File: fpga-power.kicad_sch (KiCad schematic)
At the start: 81 parts, among them U15 XC7K160T-FFG676

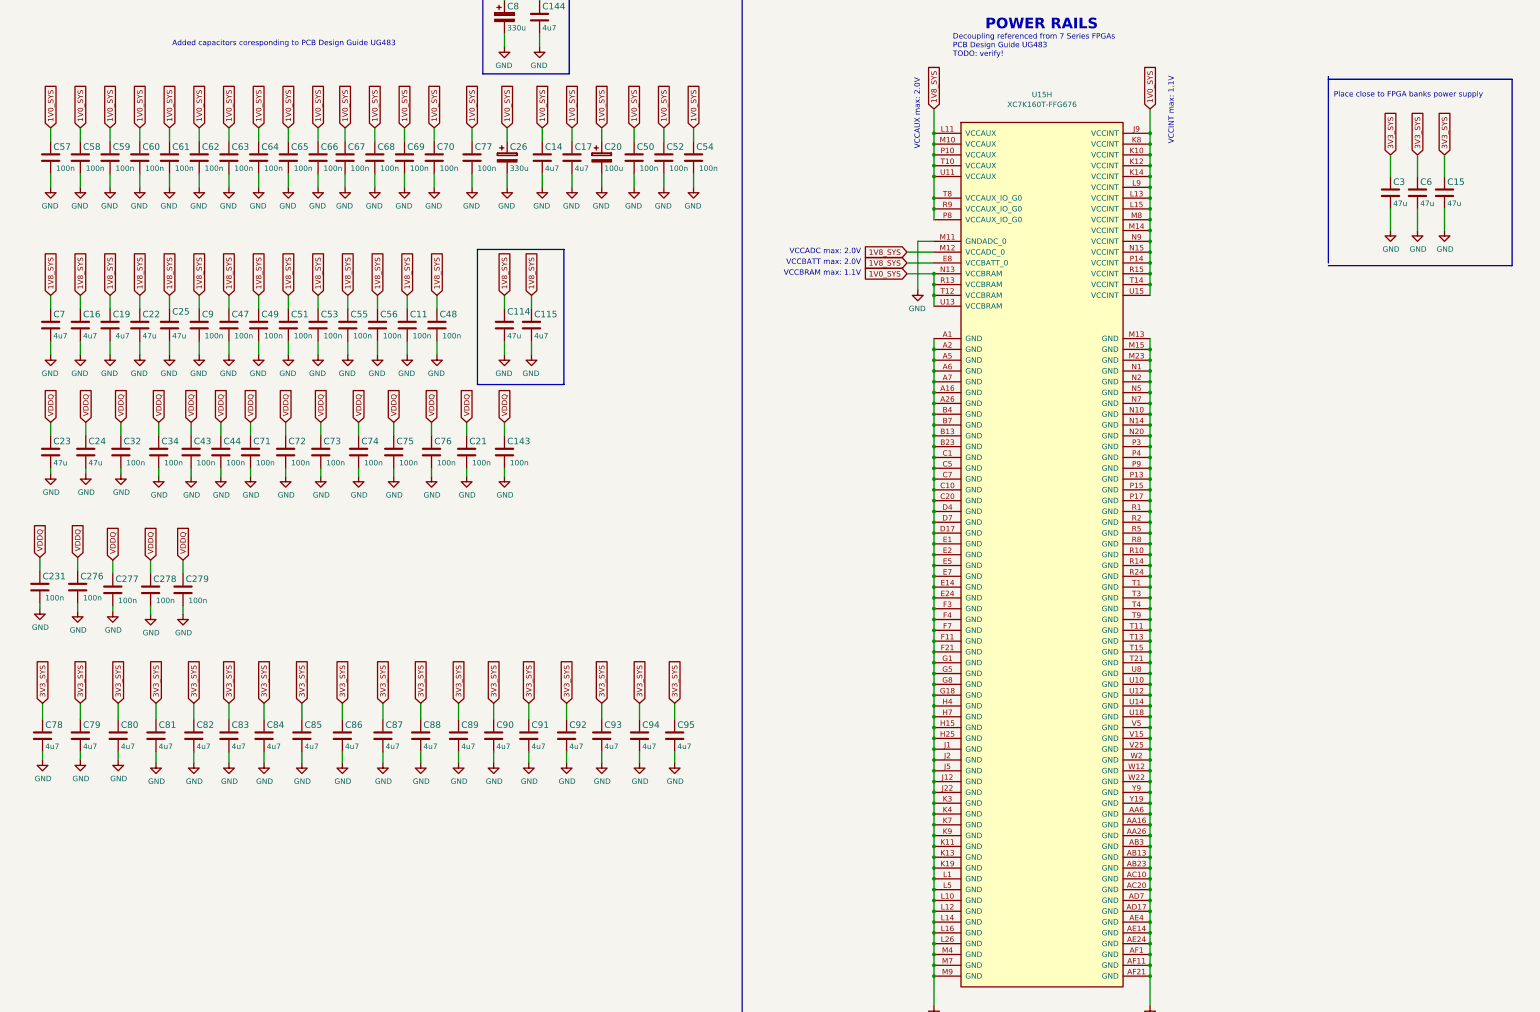
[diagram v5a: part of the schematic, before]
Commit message: Assign and connect misc. signals. Add, place and route decoupling capacitors
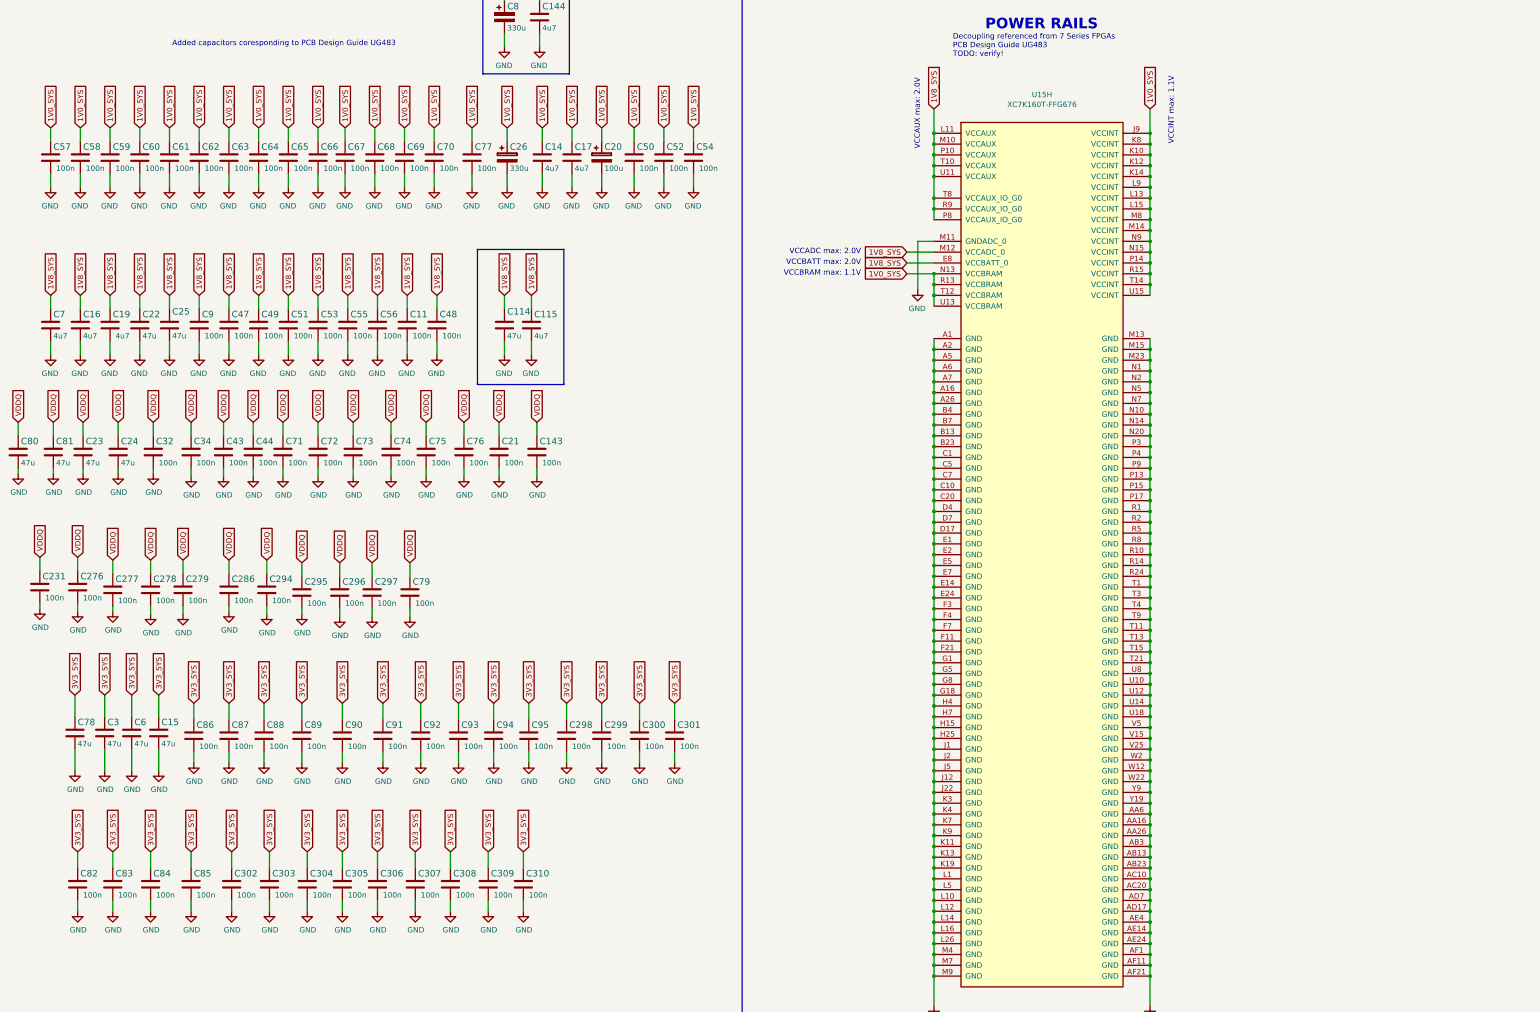
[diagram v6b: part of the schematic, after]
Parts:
- removed C78, C79, C80, C81, C82, C83, C84, C85, C86, C87, C88, C89, C90, C91, C92, C93, C94, C95: C_4u7_0402, data-center-dram-tester-footprints:0402-cap, symbol data-center-dram-tester:C_4u7_0402
- added C286, C294, C295, C296, C297, C298, C299, C300, C301, C302, C303, C304, C305, C306, C307, C308, C309, C310, C79, C82, C83, C84, C85, C86, C87, C88, C89, C90, C91, C92, C93, C94, C95: C_100n_0201, data-center-dram-tester-footprints:0201-res, symbol data-center-dram-tester:C_100n_0201
- added C78, C80, C81: C_47u_0603, data-center-dram-tester-footprints:0603-cap, symbol data-center-dram-tester:C_47u_0603
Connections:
- net 3V3_SYS: now also C298.1, C299.1, C300.1, C301.1, C302.1, C303.1, C304.1, C305.1, C306.1, C307.1, C308.1, C309.1, C310.1, C78.1, C82.1, C83.1, C84.1, C85.1, C86.1, C87.1, C88.1, C89.1, C90.1, C91.1, C92.1, C93.1, C94.1, C95.1
- net GND: now also C286.2, C294.2, C295.2, C296.2, C297.2, C298.2, C299.2, C300.2, C301.2, C302.2, C303.2, C304.2, C305.2, C306.2, C307.2, C308.2, C309.2, C310.2, C78.2, C79.2, C80.2, C81.2, C82.2, C83.2, C84.2, C85.2, C86.2, C87.2, C88.2, C89.2, C90.2, C91.2, C92.2, C93.2, C94.2, C95.2
- net VDDQ: now also C286.1, C294.1, C295.1, C296.1, C297.1, C79.1, C80.1, C81.1
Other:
- note removed: "Place close to FPGA banks power supply"
- moved on the sheet: C143, C15, C21, C23, C24, C3, C32, C34, C43, C44, C6, C71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

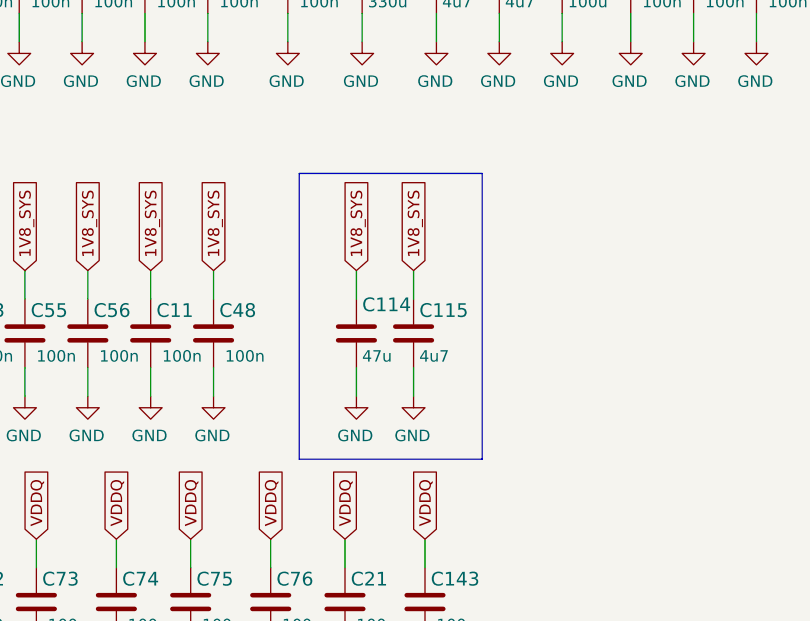
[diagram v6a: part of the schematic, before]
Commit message: Readability improvements
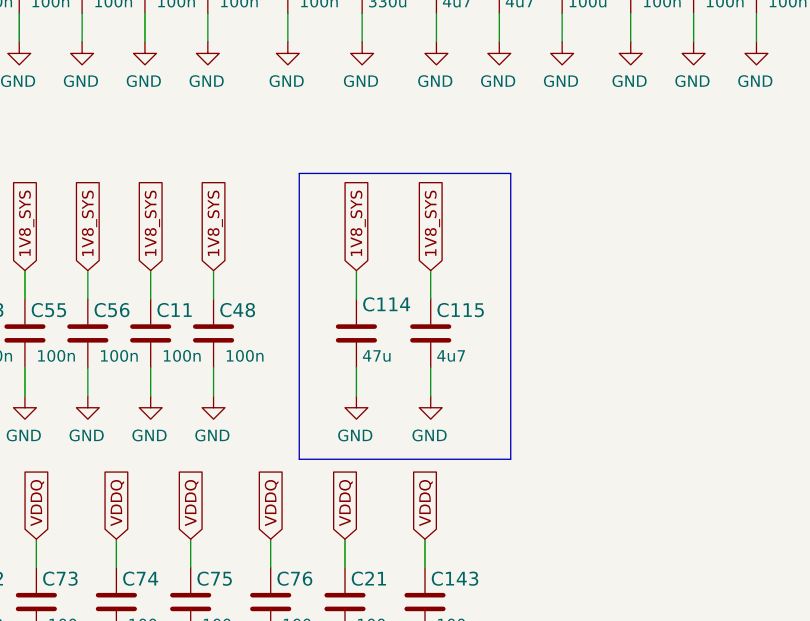
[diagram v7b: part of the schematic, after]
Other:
- moved on the sheet: C115
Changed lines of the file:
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@@
     (stroke (width 0) (type default) (color 0 0 0 0))
   )
-  (polyline (pts (xy 128.905 90.17) (xy 149.225 90.17))
+  (polyline (pts (xy 128.905 90.17) (xy 152.4 90.17))
     (stroke (width 0) (type default) (color 0 0 0 0))
   )
@@
     (stroke (width 0) (type default) (color 0 0 0 0))
   )
-  (polyline (pts (xy 149.225 121.92) (xy 128.905 121.92))
+  (polyline (pts (xy 152.4 121.92) (xy 128.905 121.92))
     (stroke (width 0) (type default) (color 0 0 0 0))
   )
@@
     (stroke (width 0) (type default) (color 0 0 0 0))
   )
-  (wire (pts (xy 141.605 104.14) (xy 141.605 100.965))
+  (wire (pts (xy 143.51 104.14) (xy 143.51 100.965))
     (stroke (width 0) (type default) (color 0 0 0 0))
   )
@@
     (stroke (width 0) (type default) (color 0 0 0 0))
   )
-  (polyline (pts (xy 149.225 90.17) (xy 149.225 121.92))
+  (polyline (pts (xy 152.4 90.17) (xy 152.4 121.92))
     (stroke (width 0) (type default) (color 0 0 0 0))
   )
@@
     (stroke (width 0) (type default) (color 0 0 0 0))
   )
-  (wire (pts (xy 141.605 114.935) (xy 141.605 111.76))
+  (wire (pts (xy 143.51 114.935) (xy 143.51 111.76))
     (stroke (width 0) (type default) (color 0 0 0 0))
   )
@@
     )
   )
-  (global_label "1V8_SYS" (shape input) (at 141.605 100.965 90) (fields_autoplaced)
+  (global_label "1V8_SYS" (shape input) (at 143.51 100.965 90) (fields_autoplaced)
     (effects (font (size 1.27 1.27)) (justify left))
-    (property "Intersheet References" "${INTERSHEET_REFS}" (id 0) (at -0.635 -45.72 0)
+    (property "Intersheet References" "${INTERSHEET_REFS}" (id 0) (at 1.27 -45.72 0)
       (effects (font (size 1.27 1.27)) hide)
     )
@@
     (pin "1")
   )
-  (symbol (lib_id "data-center-dram-tester:C_4u7_0402") (at 141.605 107.95 0) (unit 1)
+  (symbol (lib_id "data-center-dram-tester:C_4u7_0402") (at 143.51 107.95 0) (unit 1)
     (in_bom yes) (on_board yes)
-    (property "Reference" "C115" (id 0) (at 142.24 105.41 0)
+    (property "Reference" "C115" (id 0) (at 144.145 105.41 0)
       (effects (font (size 1.524 1.524)) (justify left))
     )
-    (property "Value" "C_4u7_0402" (id 1) (at 141.605 111.76 0)
+    (property "Value" "C_4u7_0402" (id 1) (at 143.51 111.76 0)
       (effects (font (size 1.524 1.524)) hide)
     )
-    (property "Footprint" "data-center-dram-tester-footprints:0402-cap" (id 2) (at 146.685 102.87 0)
+    (property "Footprint" "data-center-dram-tester-footprints:0402-cap" (id 2) (at 148.59 102.87 0)
       (effects (font (size 1.524 1.524)) (justify left) hide)
     )
-    (property "Datasheet" "" (id 3) (at 141.605 107.95 0)
+    (property "Datasheet" "" (id 3) (at 143.51 107.95 0)
       (effects (font (size 1.27 1.27)) hide)
     )
-    (property "Manufacturer" "MURATA" (id 4) (at 146.685 97.79 0)
+    (property "Manufacturer" "MURATA" (id 4) (at 148.59 97.79 0)
       (effects (font (size 1.524 1.524)) (justify left) hide)
     )
-    (property "MPN" "GRM155R61A475MEAAD" (id 5) (at 146.685 100.33 0)
+    (property "MPN" "GRM155R61A475MEAAD" (id 5) (at 148.59 100.33 0)
       (effects (font (size 1.524 1.524)) (justify left) hide)
     )
-    (property "Val" "4u7" (id 6) (at 142.24 110.49 0)
+    (property "Val" "4u7" (id 6) (at 144.145 110.49 0)
       (effects (font (size 1.27 1.27)) (justify left))
     )
@@
     (pin "2")
   )
-  (symbol (lib_id "data-center-dram-tester:GND") (at 141.605 114.935 0) (mirror y) (unit 1)
+  (symbol (lib_id "data-center-dram-tester:GND") (at 143.51 114.935 0) (mirror y) (unit 1)
     (in_bom yes) (on_board yes)
-    (property "Reference" "#PWR0108" (id 0) (at 141.605 121.285 0)
+    (property "Reference" "#PWR0108" (id 0) (at 143.51 121.285 0)
       (effects (font (size 1.27 1.27)) hide)
     )
-    (property "Value" "GND" (id 1) (at 141.478 119.3292 0))
-    (property "Footprint" "" (id 2) (at 141.605 114.935 0)
+    (property "Value" "GND" (id 1) (at 143.383 119.3292 0))
+    (property "Footprint" "" (id 2) (at 143.51 114.935 0)
       (effects (font (size 1.27 1.27)) hide)
     )
-    (property "Datasheet" "" (id 3) (at 141.605 114.935 0)
+    (property "Datasheet" "" (id 3) (at 143.51 114.935 0)
       (effects (font (size 1.27 1.27)) hide)
     )

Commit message: Final touches
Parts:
- added C313: C_100n_0402, antmicro-footprints:0402-cap, symbol antmicroCapacitors0402:C_100n_0402
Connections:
- net GND: now also C313.2
- net VDDQ: now also C313.1
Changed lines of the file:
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@@
     (stroke (width 0) (type default) (color 0 0 0 0))
   )
+  (wire (pts (xy 159.385 130.175) (xy 159.385 133.35))
+    (stroke (width 0) (type default) (color 0 0 0 0))
+  )
   (wire (pts (xy 104.14 163.83) (xy 104.14 167.005))
     (stroke (width 0) (type default) (color 0 0 0 0))
@@
     (stroke (width 0) (type default) (color 0 0 0 0))
   )
+  (wire (pts (xy 159.385 140.97) (xy 159.385 142.875))
+    (stroke (width 0) (type default) (color 0 0 0 0))
+  )
   (wire (pts (xy 236.22 238.125) (xy 236.22 240.665))
     (stroke (width 0) (type default) (color 0 0 0 0))
@@
     )
   )
+  (global_label "VDDQ" (shape input) (at 159.385 130.175 90) (fields_autoplaced)
+    (effects (font (size 1.27 1.27)) (justify left))
+    (property "Intersheet References" "${INTERSHEET_REFS}" (id 0) (at 23.495 -46.355 0)
+      (effects (font (size 1.27 1.27)) hide)
+    )
+  )
   (global_label "1V8_SYS" (shape input) (at 42.545 100.965 90) (fields_autoplaced)
     (effects (font (size 1.27 1.27)) (justify left))
@@
     (pin "2")
   )
+  (symbol (lib_id "antmicroCapacitors0402:C_100n_0402") (at 159.385 137.16 0) (unit 1)
+    (in_bom yes) (on_board yes) (fields_autoplaced)
+    (property "Reference" "C313" (id 0) (at 162.306 136.3254 0)
+      (effects (font (size 1.524 1.524)) (justify left))
+    )
+    (property "Value" "C_100n_0402" (id 1) (at 159.385 140.97 0)
+      (effects (font (size 1.524 1.524)) hide)
+    )
+    (property "Footprint" "antmicro-footprints:0402-cap" (id 2) (at 164.465 132.08 0)
+      (effects (font (size 1.524 1.524)) (justify left) hide)
+    )
+    (property "Datasheet" "" (id 3) (at 159.385 137.16 0)
+      (effects (font (size 1.27 1.27)) hide)
+    )
+    (property "Manufacturer" "Murata" (id 4) (at 164.465 127 0)
+      (effects (font (size 1.524 1.524)) (justify left) hide)
+    )
+    (property "MPN" "GRM155R61H104KE14D" (id 5) (at 164.465 129.54 0)
+      (effects (font (size 1.524 1.524)) (justify left) hide)
+    )
+    (property "Val" "100n" (id 6) (at 162.306 139.0905 0)
+      (effects (font (size 1.27 1.27)) (justify left))
+    )
+    (pin "1")
+    (pin "2")
+  )
   (symbol (lib_id "data-center-dram-tester:C_100n_0201") (at 115.57 204.47 0) (unit 1)
     (in_bom yes) (on_board yes)
@@
       (effects (font (size 1.27 1.27)) hide)
     )
+    (pin "1")
+  )
+  (symbol (lib_id "data-center-dram-tester:GND") (at 159.385 142.875 0) (unit 1)
+    (in_bom yes) (on_board yes)
+    (property "Reference" "#PWR0397" (id 0) (at 159.385 149.225 0)
+      (effects (font (size 1.27 1.27)) hide)
+    )
+    (property "Value" "GND" (id 1) (at 159.512 147.2692 0))
+    (property "Footprint" "" (id 2) (at 159.385 142.875 0)
+      (effects (font (size 1.27 1.27)) hide)
+    )
+    (property "Datasheet" "" (id 3) (at 159.385 142.875 0)
+      (effects (font (size 1.27 1.27)) hide)
+    )
